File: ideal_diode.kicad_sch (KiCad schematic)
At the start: 4 parts, among them Q1 Q_NMOS_DSG, U9 LTC4357DCB

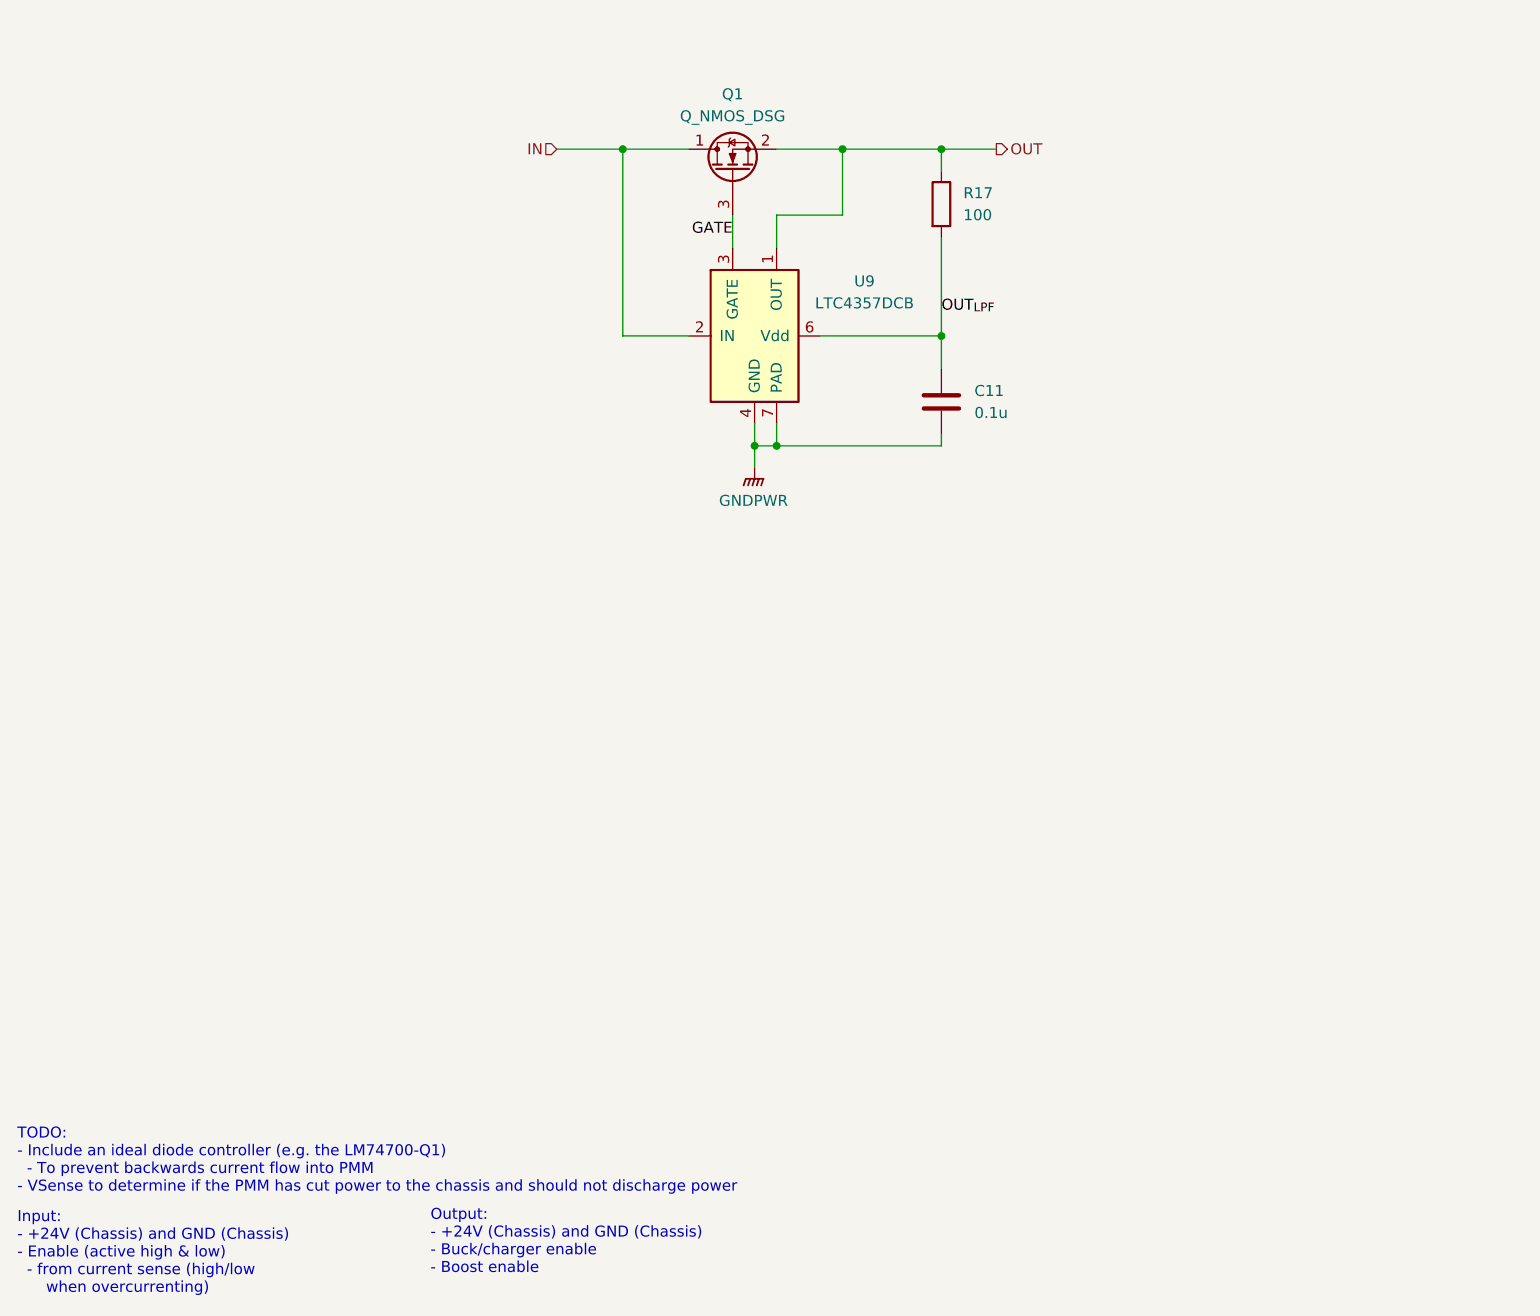
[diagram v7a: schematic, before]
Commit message: Add in voltage control for components
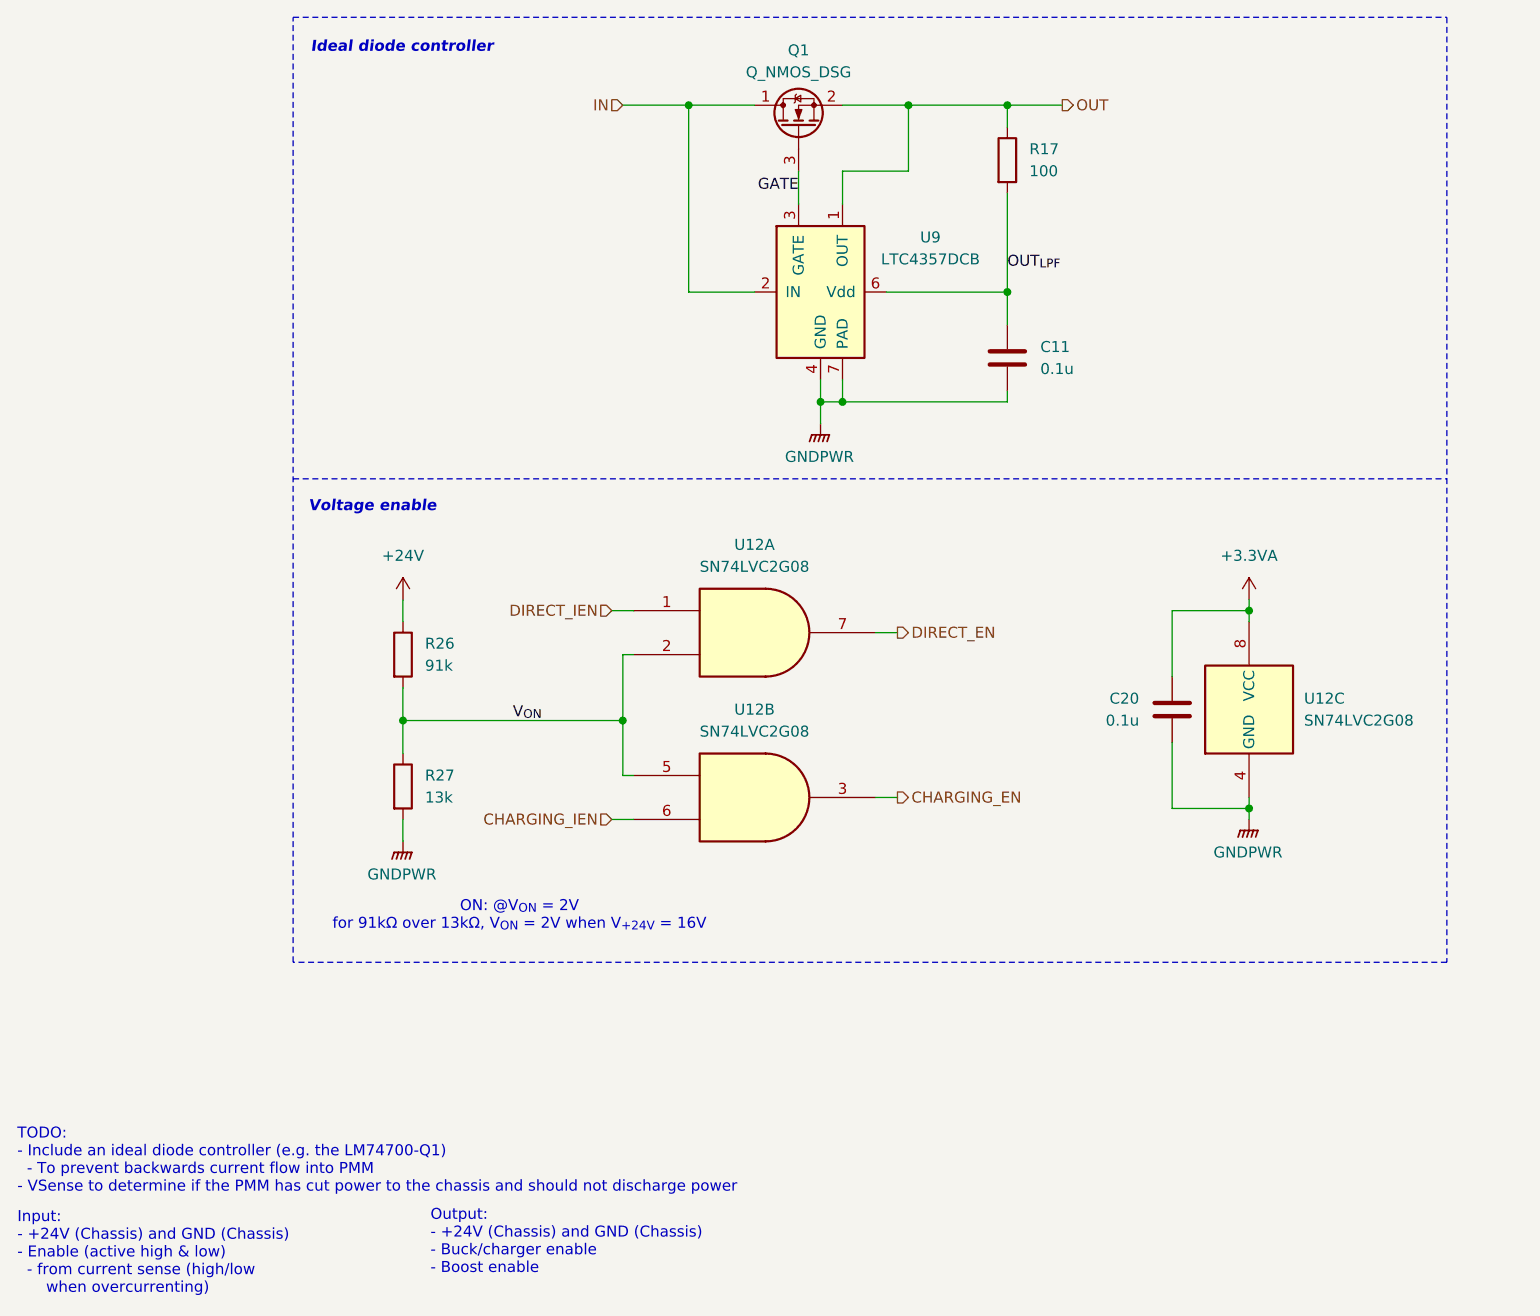
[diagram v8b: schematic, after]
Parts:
- added C20: 0.1u, Capacitor_SMD:C_0603_1608Metric_Pad1.08x0.95mm_HandSolder, symbol Device:C
- added R26: 91k, Resistor_SMD:R_0603_1608Metric_Pad0.98x0.95mm_HandSolder, symbol Device:R
- added R27: 13k, Resistor_SMD:R_0603_1608Metric_Pad0.98x0.95mm_HandSolder, symbol Device:R
- added U12: SN74LVC2G08, Package_SO:VSSOP-8_2.3x2mm_P0.5mm, symbol ! Robomaster ICs:SN74LVC2G08
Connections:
- net GNDPWR: now also C20.2, R27.2, U12.4 (GND)
- new net +24V: R26.1
- new net +3.3VA: C20.1, U12.8 (VCC)
- new net CHARGING_EN: U12.3
- new net CHARGING_IEN: U12.6
- new net DIRECT_EN: U12.7
- new net DIRECT_IEN: U12.1
- new net V_{ON}: R26.2, R27.1, U12.2, U12.5
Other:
- note added: "Ideal diode controller"
- note added: "ON: @V_{ON} = 2V for 91kΩ over 13kΩ, V_{ON} = 2V when V_{+24V} = 16V"
- note added: "Voltage enable"
- moved on the sheet: C11, Q1, R17, U9
